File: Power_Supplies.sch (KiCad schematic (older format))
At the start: 83 parts, among them IC2 MAX809LEUR+, IC3 TPS74801TDRCRQ1, IC4 ADP1715ARMZ-3.3-R7, IC5 ADP1715ARMZ-3.3-R7, J1 Conn_HDR_2x10_latching, M1 2N7002BK, M2 2N7002BK, Q11 2N7002BK, Q12 2N7002BK, Q13 2N7002BK, Q14 2N7002BK, Q6 2N7002BK, Q7 2N7002BK, Q8 2N7002BK, Q9 2N7002BK, U22 BD50FC0WEFJ-E2, U23 LDL212D33R, U24 BD50FC0WEFJ-E2

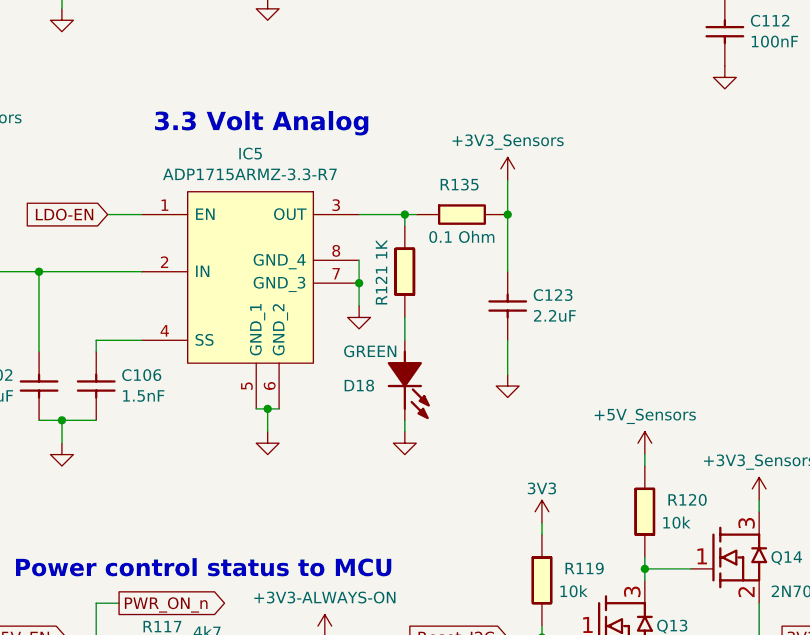
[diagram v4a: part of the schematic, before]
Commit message: footprint added to 99%
99% of parts have footprint now.
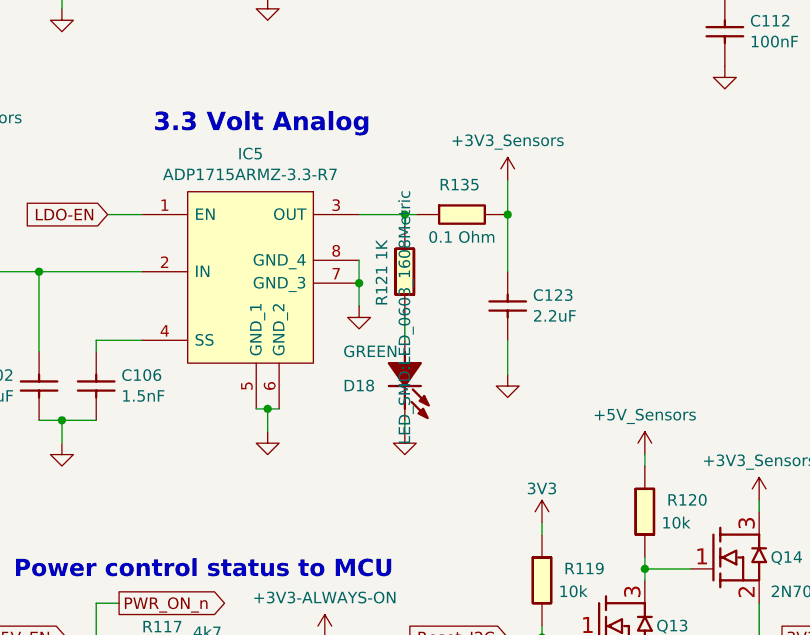
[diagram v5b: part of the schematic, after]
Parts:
- D18: footprint (none) -> LED_SMD:LED_0603_1608Metric
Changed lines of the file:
@@
 F 0 "D18" V 6950 4550 50  0000 C CNN
 F 1 "LED_GREEN_0603_SMD" H 6650 4750 60  0001 C CNN
-F 2 "" H 6650 4750 50  0000 C CNN
+F 2 "LED_SMD:LED_0603_1608Metric" H 6650 4750 50  0000 C CNN
 F 3 "" H 6650 4750 50  0000 C CNN
 F 4 "GREEN" V 6800 4600 50  0000 C CNN "Val"

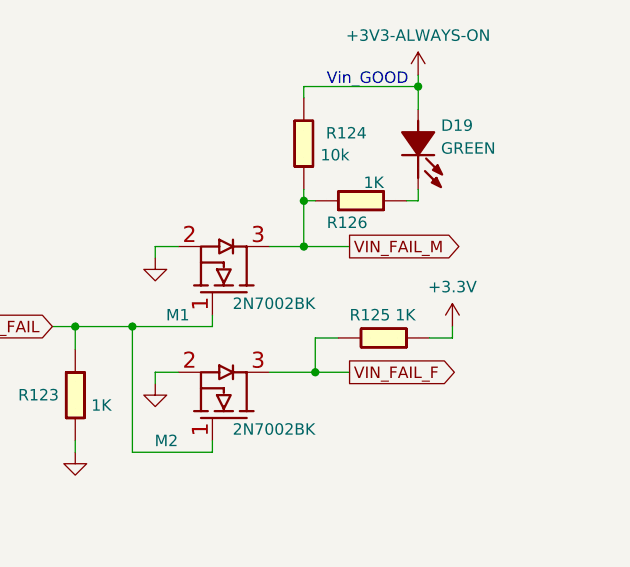
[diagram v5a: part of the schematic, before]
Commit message: Updated the project to include a M2GL010-1TQG144 IGLOO2 FPGA instead of the GOWIN. Since the IGLOO has some 2.5V BANKs as well as 3.3V Banks, some circuitry will need to be modified elsewhere in the circuit, but most of the interfaces are easily changeable, be it different power supplies or the additions of transistors or potential dividers. I will edit the rest of the design later, and write up a list of things I changed for the other peeps in the design team to review
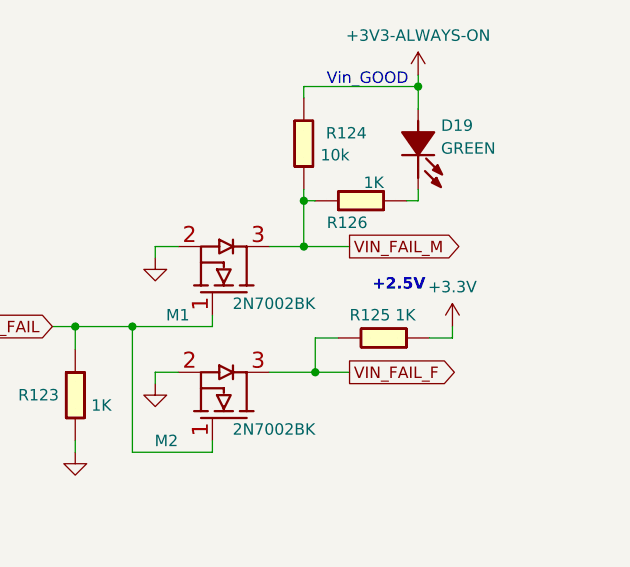
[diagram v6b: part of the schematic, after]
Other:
- note added: "+2.5V"
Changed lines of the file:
@@
 EESchema Schematic File Version 4
-EELAYER 30 0
+LIBS:OpenVent-cache
+EELAYER 26 0
 EELAYER END
 $Descr A4 11693 8268
 encoding utf-8
-Sheet 8 8
+Sheet 8 9
 Title "OpenVent Control Board"
 Date "2020-10-20"
@@
 	650  4200 650  4500
 NoConn ~ 10050 1500
+Text Notes 10600 5650 0    50   ~ 10
++2.5V
 $EndSCHEMATC

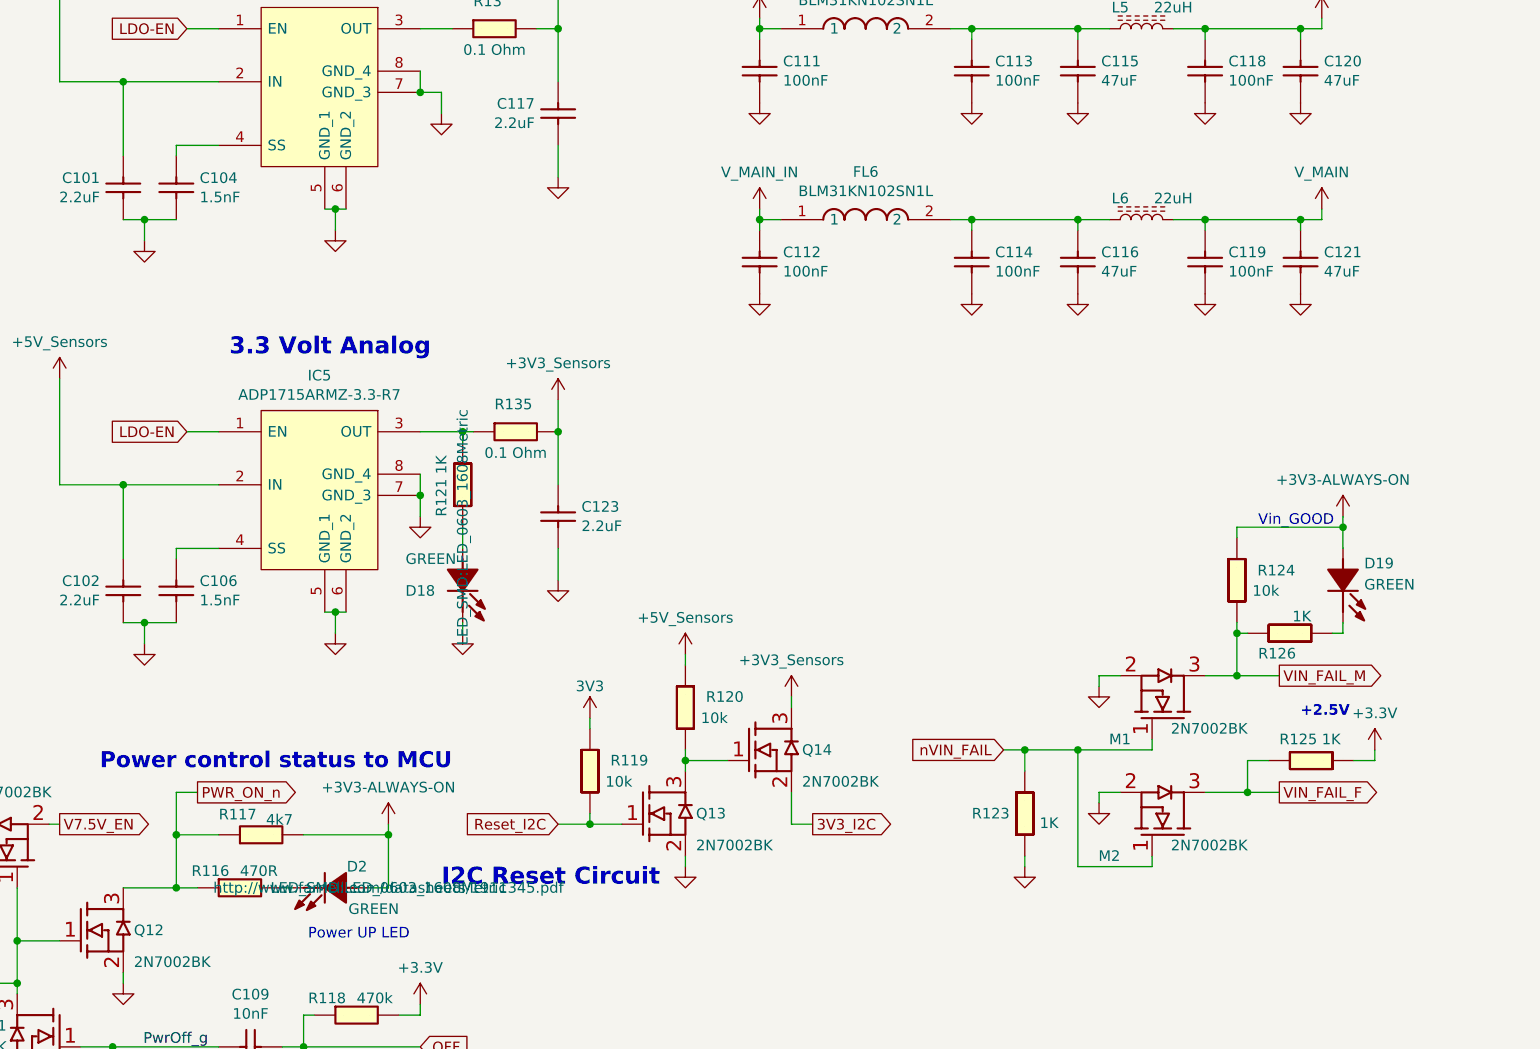
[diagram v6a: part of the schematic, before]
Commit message: Finalised most of the schematic. I think there are a few more things to do in the Speaker
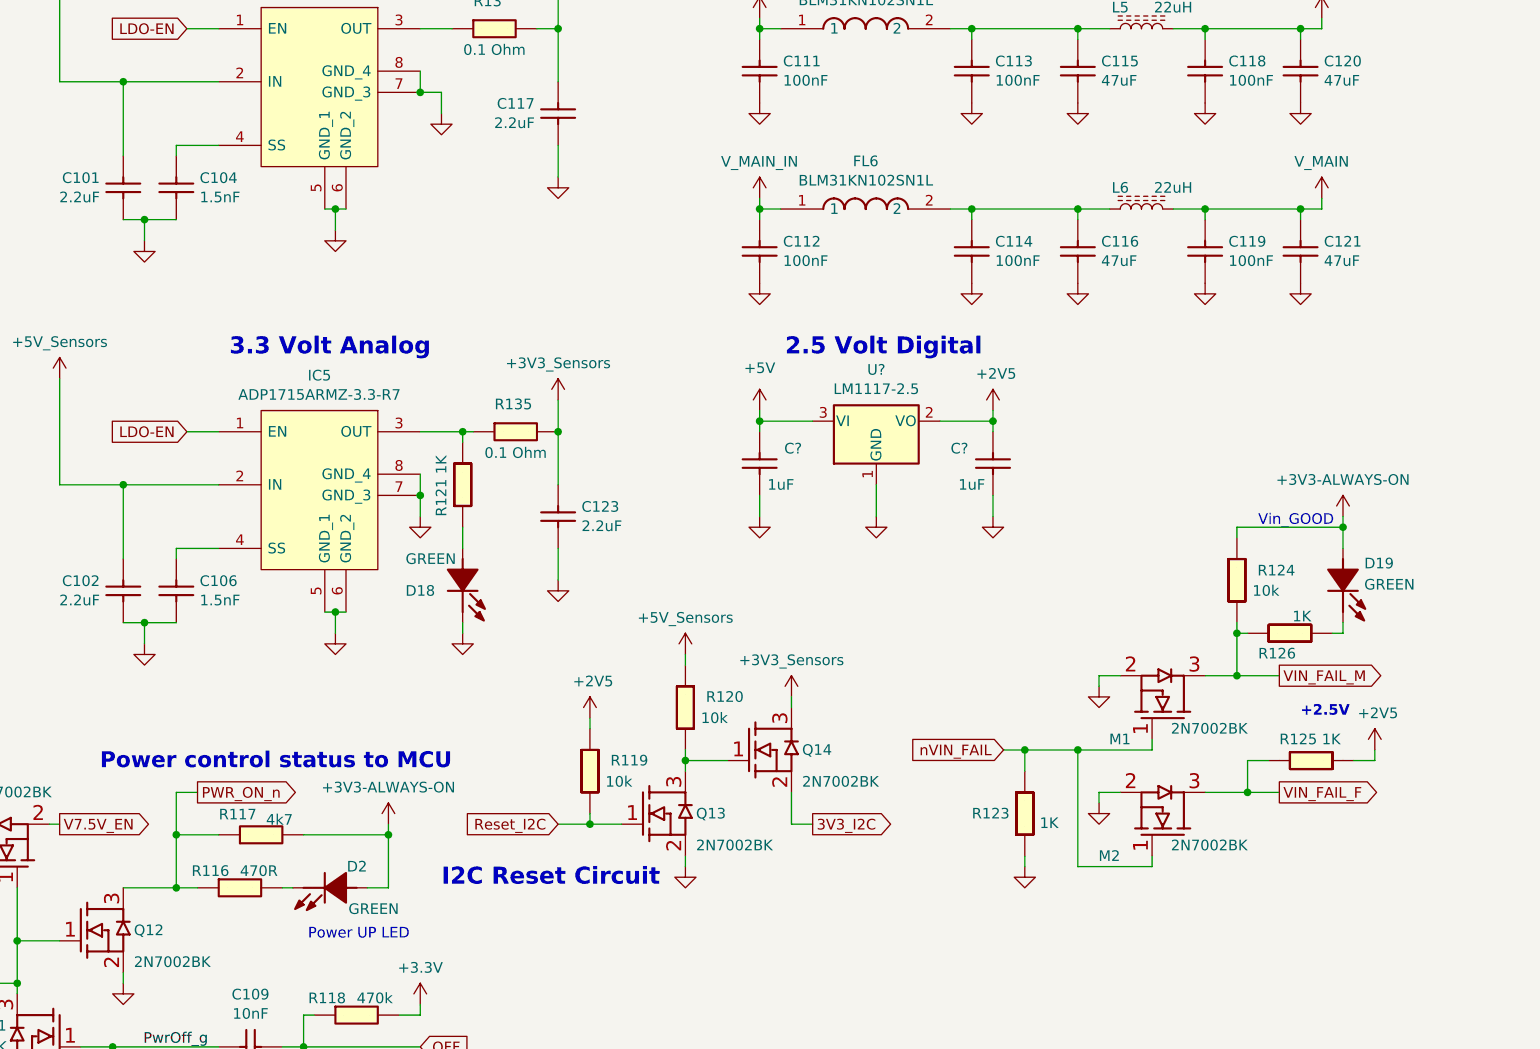
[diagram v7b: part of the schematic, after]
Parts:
- added C? (x2): 1uF_0603_Ceramic_Capacitor,_10%,_50V,_X5R, Capacitor_SMD:C_0603_1608Metric, symbol OpenVent:1uF_0603_Ceramic_Capacitor,_10%,_50V,_X5R
- added U?: LM1117-2.5, symbol Regulator_Linear:LM1117-2.5
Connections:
- net +3V3: no longer R119.2, R125.2
- net +5V: now also C?.2, U?.3 (VI)
- net GND: now also C?.1, C?.1, U?.1 (GND)
- new net +2V5: C?.2, R119.2, R125.2, U?.2 (VO)
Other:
- note added: "2.5 Volt Digital"
- moved on the sheet: C112, C114, C116, C119, C121, FL6, L6
